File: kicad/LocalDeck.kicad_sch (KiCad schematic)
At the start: 26 parts, among them IC1 ESP32-C3-MINI-1-N4, J1 Conn_01x02_Pin, P1 USB_C_Receptacle_USB2.0, P2 USB_C_Receptacle_USB2.0, SW1 Boot, U1 AMS1117-3.3

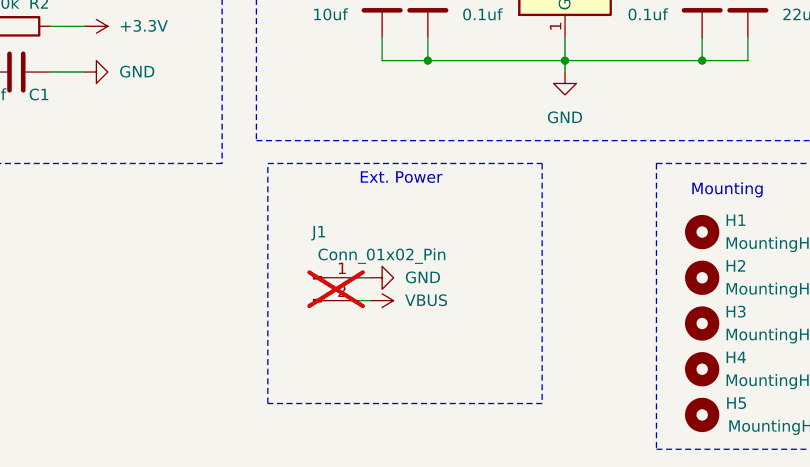
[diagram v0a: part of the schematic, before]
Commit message: feat: Added programming Header
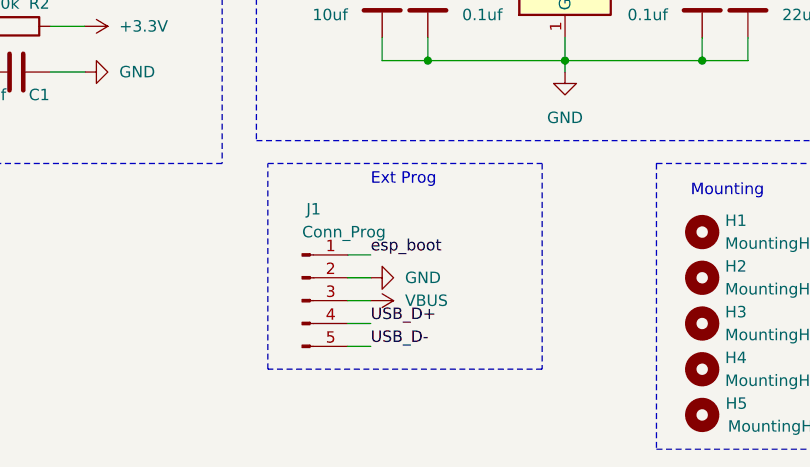
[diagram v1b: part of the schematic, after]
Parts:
- removed J1: Conn_01x02_Pin, Connector_PinHeader_2.54mm:PinHeader_1x02_P2.54mm_Vertical, symbol Connector:Conn_01x02_Pin
- added J1: Conn_Prog, LocalDeck Custom:ProgrammingHeader, symbol Connector:Conn_01x05_Pin
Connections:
- net GND: now also J1.2 (Pin_2)
- net USB_D+: now also J1.4 (Pin_4)
- net USB_D-: now also J1.5 (Pin_5)
- net VBUS: now also J1.3 (Pin_3)
- net esp_boot: now also J1.1 (Pin_1)
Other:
- note added: "Ext Prog"
- note removed: "Ext. Power"

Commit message: chore(kicad): Added measurements & part numbers
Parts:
- D1: JLC Part (none) -> C3018529
- H1, H2, H3, H4, H5, J1: now left out of the parts list
- SW1: JLC Part (none) -> C318884
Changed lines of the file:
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@@
   )
   (symbol (lib_id "Connector:Conn_01x05_Pin") (at 217.17 119.38 0) (unit 1)
-    (in_bom yes) (on_board yes) (dnp no)
+    (in_bom no) (on_board yes) (dnp no)
     (property "Reference" "J1" (at 218.44 109.22 0)
       (effects (font (size 1.27 1.27)))
@@
   )
   (symbol (lib_id "Mechanical:MountingHole") (at 261.62 132.08 90) (unit 1)
-    (in_bom yes) (on_board yes) (dnp no)
+    (in_bom no) (on_board yes) (dnp no)
     (property "Reference" "H5" (at 265.43 130.81 90)
       (effects (font (size 1.27 1.27)))
@@
       (effects (font (size 1.27 1.27)) hide)
     )
-    (property "JLC Part" "" (at 219.71 77.47 0)
+    (property "JLC Part" "C3018529" (at 219.71 77.47 0)
       (effects (font (size 1.27 1.27)) hide)
     )
@@
   )
   (symbol (lib_id "Mechanical:MountingHole") (at 261.62 111.76 270) (unit 1)
-    (in_bom yes) (on_board yes) (dnp no) (fields_autoplaced)
+    (in_bom no) (on_board yes) (dnp no) (fields_autoplaced)
     (property "Reference" "H1" (at 264.16 110.49 90)
       (effects (font (size 1.27 1.27)) (justify left))
@@
       (effects (font (size 1.27 1.27)) hide)
     )
-    (property "JLC Part" "" (at 185.42 83.82 0)
+    (property "JLC Part" "C318884" (at 185.42 83.82 0)
       (effects (font (size 1.27 1.27)) hide)
     )
@@
   )
   (symbol (lib_id "Mechanical:MountingHole") (at 261.62 121.92 270) (unit 1)
-    (in_bom yes) (on_board yes) (dnp no) (fields_autoplaced)
+    (in_bom no) (on_board yes) (dnp no) (fields_autoplaced)
     (property "Reference" "H3" (at 264.16 120.65 90)
       (effects (font (size 1.27 1.27)) (justify left))
@@
   )
   (symbol (lib_id "Mechanical:MountingHole") (at 261.62 127 270) (unit 1)
-    (in_bom yes) (on_board yes) (dnp no) (fields_autoplaced)
+    (in_bom no) (on_board yes) (dnp no) (fields_autoplaced)
     (property "Reference" "H4" (at 264.16 125.73 90)
       (effects (font (size 1.27 1.27)) (justify left))
@@
   )
   (symbol (lib_id "Mechanical:MountingHole") (at 261.62 116.84 270) (unit 1)
-    (in_bom yes) (on_board yes) (dnp no) (fields_autoplaced)
+    (in_bom no) (on_board yes) (dnp no) (fields_autoplaced)
     (property "Reference" "H2" (at 264.16 115.57 90)
       (effects (font (size 1.27 1.27)) (justify left))
